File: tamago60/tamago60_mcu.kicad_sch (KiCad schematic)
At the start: 18 parts, among them J1 4105, J2 Cirque FFC, SW1 SW_Push, U1 ATmega32U4-A, U2 NCP1117-3.3_SOT223, Y1 16MHz

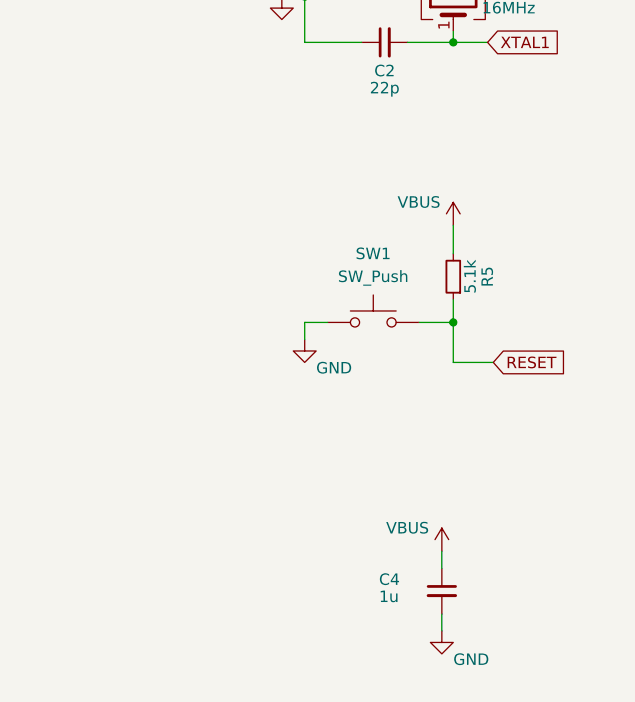
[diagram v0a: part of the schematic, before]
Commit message: route left side
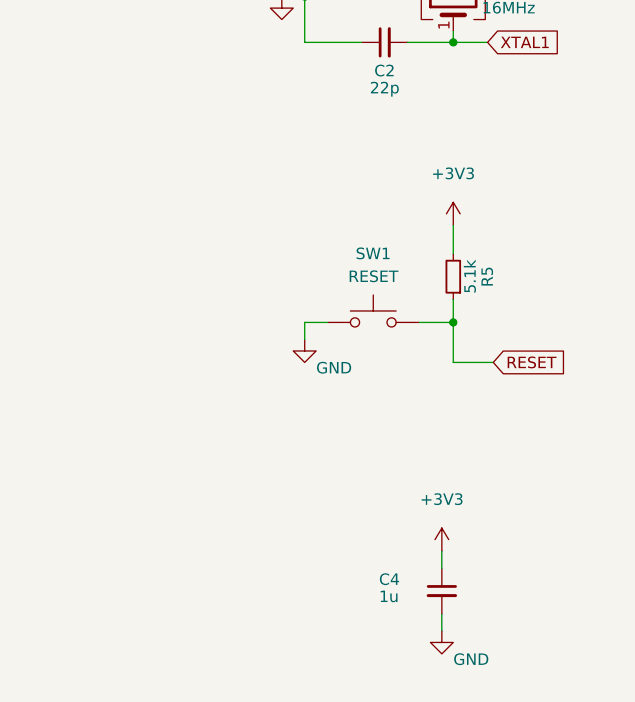
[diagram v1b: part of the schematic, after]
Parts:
- SW1: value SW_Push -> RESET
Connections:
- net +3V3: now also C4.1, R5.2
- net VBUS: no longer C4.1, R5.2
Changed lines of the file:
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@@
     )
-  )
-  (symbol (lib_id "power:VBUS") (at 229.235 55.88 0) (unit 1)
-    (in_bom yes) (on_board yes)
-    (property "Reference" "#PWR0106" (id 0) (at 229.235 59.69 0)
-      (effects (font (size 1.27 1.27)) hide)
-    )
-    (property "Value" "VBUS" (id 1) (at 225.425 53.34 0))
-    (property "Footprint" "" (id 2) (at 229.235 55.88 0)
-      (effects (font (size 1.27 1.27)) hide)
-    )
-    (property "Datasheet" "" (id 3) (at 229.235 55.88 0)
-      (effects (font (size 1.27 1.27)) hide)
-    )
-    (pin "1")
   )
   (symbol (lib_id "Device:R_Small") (at 19.685 53.975 270) (unit 1)
@@
     (in_bom yes) (on_board yes) (fields_autoplaced)
     (property "Reference" "SW1" (id 0) (at 220.345 59.055 0))
-    (property "Value" "SW_Push" (id 1) (at 220.345 61.595 0))
+    (property "Value" "RESET" (id 1) (at 220.345 61.595 0))
     (property "Footprint" "Jumper:SolderJumper-2_P1.3mm_Open_Pad1.0x1.5mm" (id 2) (at 220.345 61.595 0)
       (effects (font (size 1.27 1.27)) hide)
@@
     )
     (property "Datasheet" "" (id 3) (at 42.545 20.955 0)
+      (effects (font (size 1.27 1.27)) hide)
+    )
+    (pin "1")
+  )
+  (symbol (lib_id "power:+3V3") (at 227.965 92.075 0) (unit 1)
+    (in_bom yes) (on_board yes) (fields_autoplaced)
+    (property "Reference" "#PWR0106" (id 0) (at 227.965 95.885 0)
+      (effects (font (size 1.27 1.27)) hide)
+    )
+    (property "Value" "+3V3" (id 1) (at 227.965 86.36 0))
+    (property "Footprint" "" (id 2) (at 227.965 92.075 0)
+      (effects (font (size 1.27 1.27)) hide)
+    )
+    (property "Datasheet" "" (id 3) (at 227.965 92.075 0)
       (effects (font (size 1.27 1.27)) hide)
     )
@@
     (pin "2")
   )
+  (symbol (lib_id "power:+3V3") (at 229.235 55.88 0) (unit 1)
+    (in_bom yes) (on_board yes) (fields_autoplaced)
+    (property "Reference" "#PWR0107" (id 0) (at 229.235 59.69 0)
+      (effects (font (size 1.27 1.27)) hide)
+    )
+    (property "Value" "+3V3" (id 1) (at 229.235 50.165 0))
+    (property "Footprint" "" (id 2) (at 229.235 55.88 0)
+      (effects (font (size 1.27 1.27)) hide)
+    )
+    (property "Datasheet" "" (id 3) (at 229.235 55.88 0)
+      (effects (font (size 1.27 1.27)) hide)
+    )
+    (pin "1")
+  )
   (symbol (lib_id "power:GND") (at 227.965 139.7 0) (unit 1)
     (in_bom yes) (on_board yes) (fields_autoplaced)
@@
     (pin "2")
   )
-  (symbol (lib_id "power:VBUS") (at 227.965 92.075 0) (unit 1)
-    (in_bom yes) (on_board yes)
-    (property "Reference" "#PWR0107" (id 0) (at 227.965 95.885 0)
-      (effects (font (size 1.27 1.27)) hide)
-    )
-    (property "Value" "VBUS" (id 1) (at 224.155 89.535 0))
-    (property "Footprint" "" (id 2) (at 227.965 92.075 0)
-      (effects (font (size 1.27 1.27)) hide)
-    )
-    (property "Datasheet" "" (id 3) (at 227.965 92.075 0)
-      (effects (font (size 1.27 1.27)) hide)
-    )
-    (pin "1")
-  )
   (symbol (lib_id "power:GND") (at 227.965 100.965 0) (unit 1)

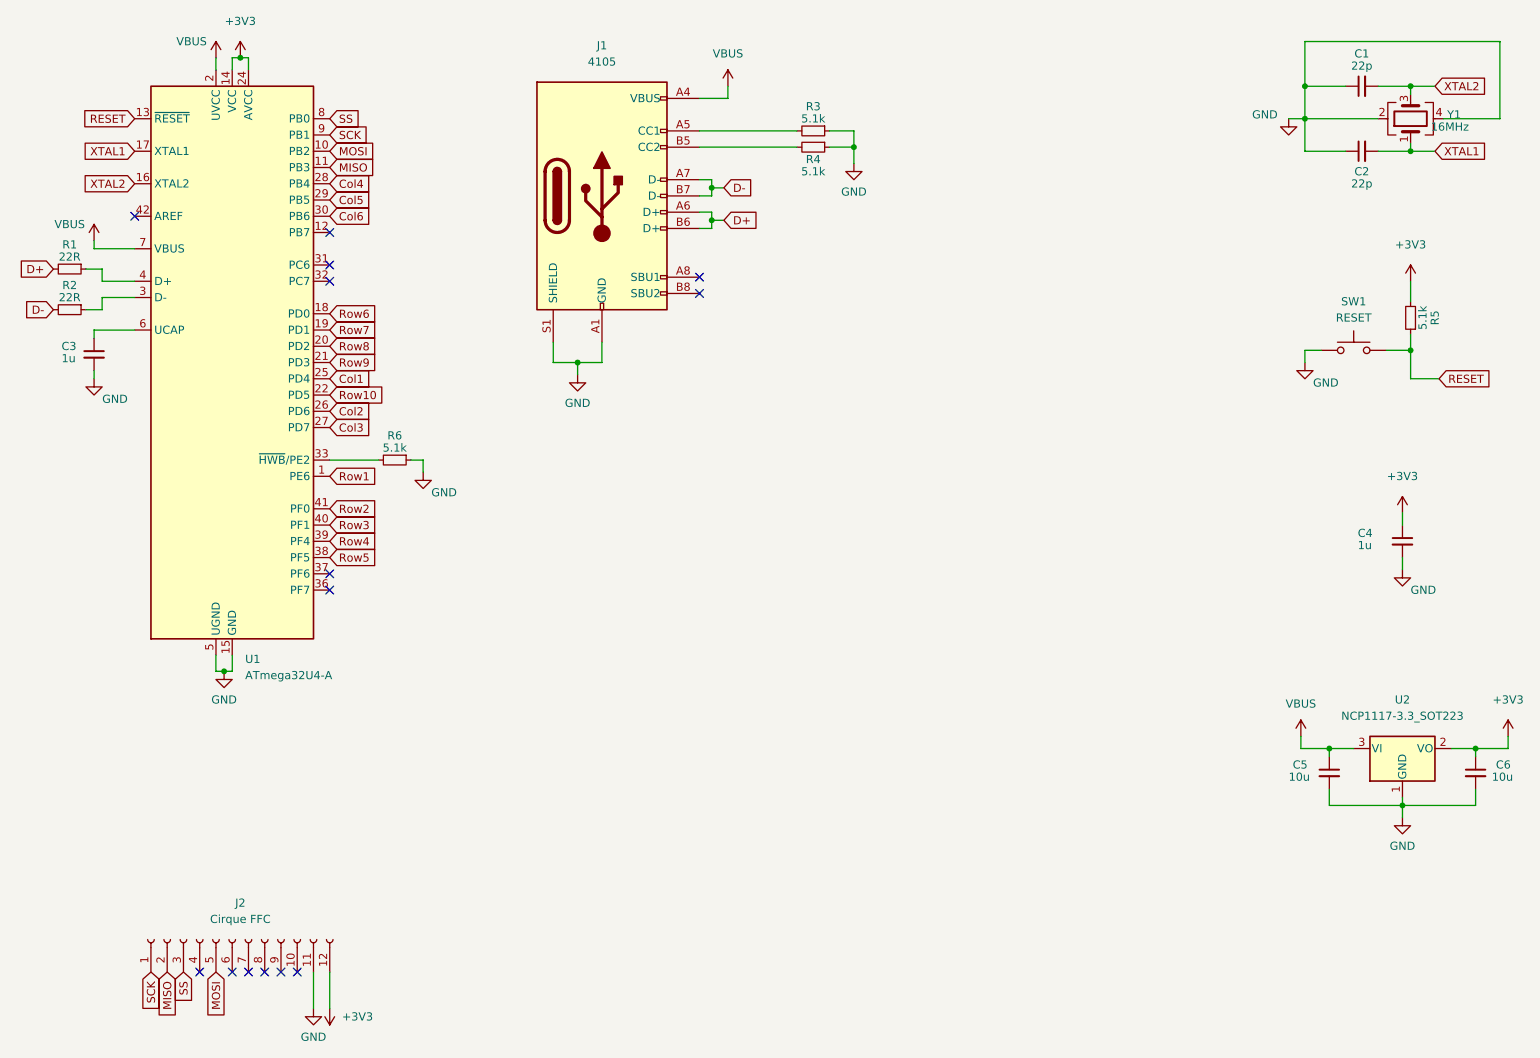
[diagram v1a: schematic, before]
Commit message: rework with rp2040 module
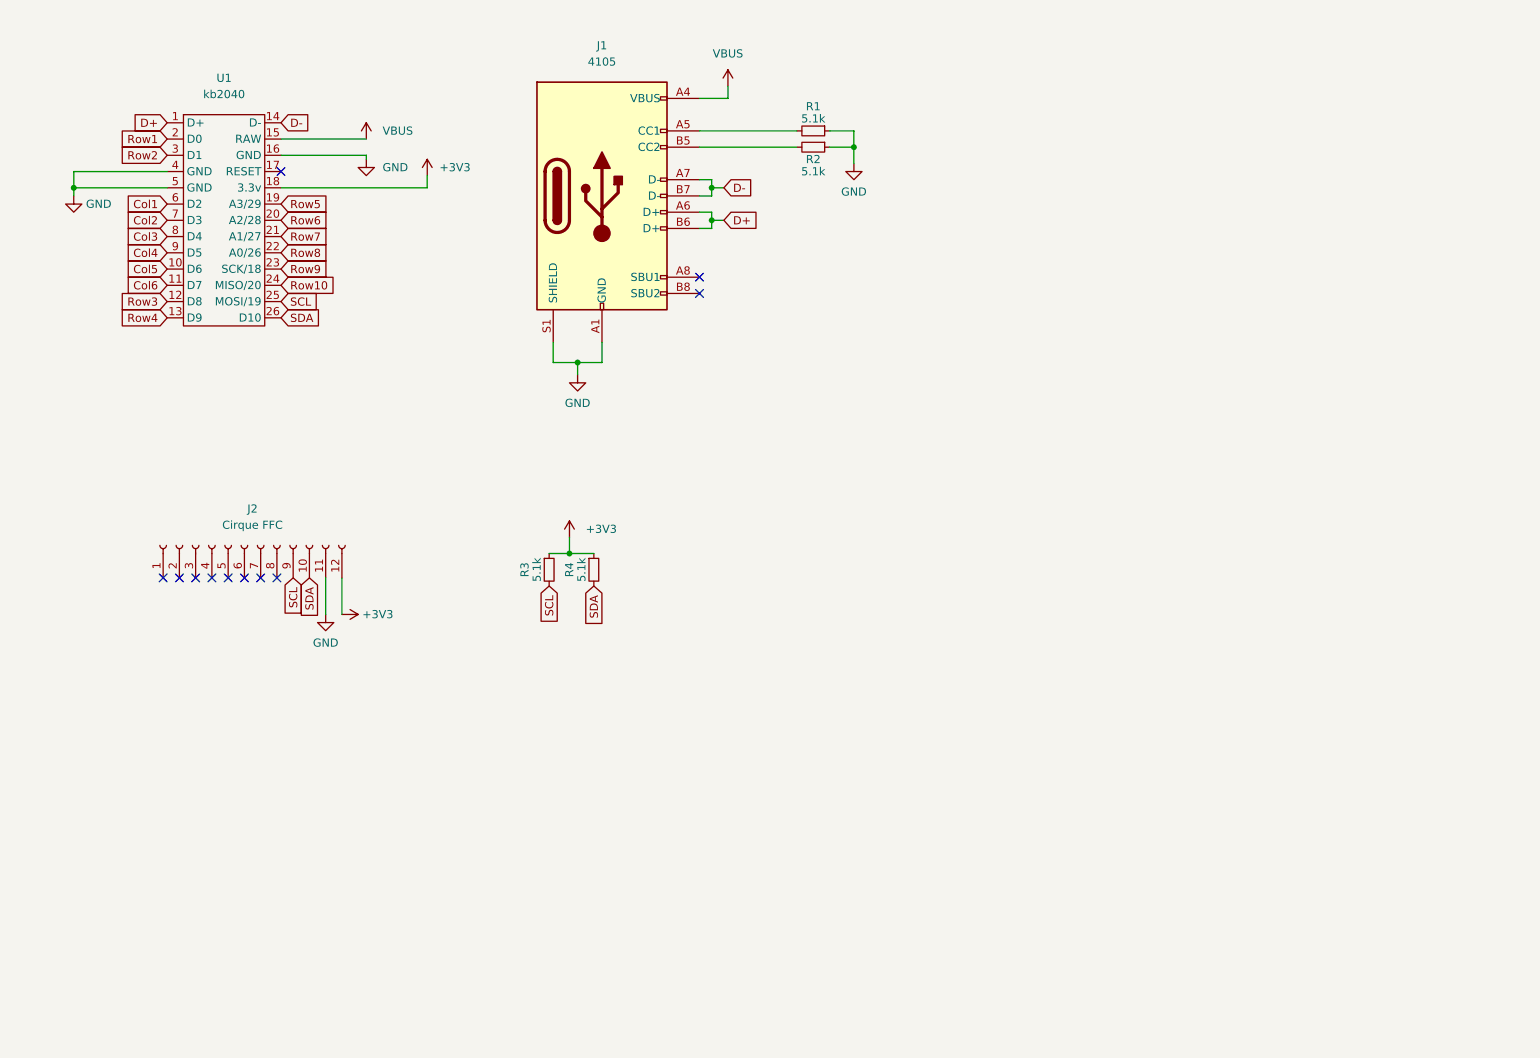
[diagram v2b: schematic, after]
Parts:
- removed C1, C2: 22p, Capacitor_SMD:C_1206_3216Metric, symbol Device:C_Small
- removed C3, C4: 1u, Capacitor_SMD:C_1206_3216Metric, symbol Device:C_Small
- removed C5, C6: 10u, Capacitor_SMD:C_1206_3216Metric, symbol Device:C_Small
- removed R1, R2: 22R, Resistor_SMD:R_1206_3216Metric, symbol Device:R_Small
- removed R5, R6: 5.1k, Resistor_SMD:R_1206_3216Metric, symbol Device:R_Small
- removed SW1: RESET, Jumper:SolderJumper-2_P1.3mm_Open_Pad1.0x1.5mm, symbol Switch:SW_Push
- removed U1: ATmega32U4-A, Package_QFP:TQFP-44_10x10mm_P0.8mm, symbol MCU_Microchip_ATmega:ATmega32U4-A
- removed U2: NCP1117-3.3_SOT223, Package_TO_SOT_SMD:SOT-223-3_TabPin2, symbol Regulator_Linear:NCP1117-3.3_SOT223
- removed Y1: 16MHz, Crystal:Crystal_SMD_2520-4Pin_2.5x2.0mm, symbol Device:Crystal_GND24
- added R3, R4: 5.1k, Resistor_SMD:R_1206_3216Metric, symbol Device:R_Small
- added U1: kb2040, kb2040:kb2040, symbol kb2040:kb2040
- renumbered R3 to R1, R4 to R2
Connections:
- net +3V3: now also R3.1, R4.1, U1.18 (3.3v)
- net Col1: now also U1.6 (D2)
- net Col2: now also U1.7 (D3)
- net Col3: now also U1.8 (D4)
- net Col4: now also U1.9 (D5)
- net Col5: now also U1.10 (D6)
- net Col6: now also U1.11 (D7)
- net D+: now also U1.1 (D+)
- net D-: now also U1.14 (D-)
- net GND: now also U1.16 (GND), U1.4 (GND), U1.5 (GND)
- net Row1: now also U1.2 (D0)
- net Row10: now also U1.24 (MISO/20)
- net Row2: now also U1.3 (D1)
- net Row3: now also U1.12 (D8)
- net Row4: now also U1.13 (D9)
- net Row5: now also U1.19 (A3/29)
- net Row6: now also U1.20 (A2/28)
- net Row7: now also U1.21 (A1/27)
- net Row8: now also U1.22 (A0/26)
- net Row9: now also U1.23 (SCK/18)
- net VBUS: now also U1.15 (RAW)
- net SDA: now reaches J2.10 (Pin_10)
- net SDA: now also R4.2, U1.26 (D10)
- net SCL: now reaches J2.9 (Pin_9)
- net SCL: now also R3.2, U1.25 (MOSI/19)
- net MISO: no longer names the net of J2.2 (Pin_2)
- net MOSI: no longer names the net of J2.5 (Pin_5)
- net SCK: no longer names the net of J2.1 (Pin_1)
- net SS: no longer names the net of J2.3 (Pin_3)
- no-connect marks 14 -> 11
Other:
- moved on the sheet: J2

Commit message: mfgr prep
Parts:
- U1: now left out of the parts list
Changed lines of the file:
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@@
   )
   (symbol (lib_id "kb2040:kb2040") (at 37.465 26.035 0) (unit 1)
-    (in_bom yes) (on_board yes) (fields_autoplaced)
+    (in_bom no) (on_board yes) (fields_autoplaced)
     (property "Reference" "U1" (id 0) (at 43.815 24.13 0))
     (property "Value" "kb2040" (id 1) (at 43.815 26.67 0))
